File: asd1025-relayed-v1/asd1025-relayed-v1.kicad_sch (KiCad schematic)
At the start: 36 parts, among them J1 Conn_01x09_Female, J10 Conn_01x01_Female, J11 Conn_01x01_Female, J12 Conn_01x01_Female, J13 Conn_01x01_Female, J14 Conn_01x01_Female, J15 Conn_01x01_Female, J16 Conn_01x01_Female, J17 Conn_01x01_Female, J18 Conn_01x01_Female, J19 Conn_01x01_Female, J2 Conn_01x01_Female, J20 Conn_01x01_Female, J21 Conn_01x01_Female, J22 Conn_01x01_Female, J3 Conn_01x01_Female, J4 Conn_01x01_Female, J5 Conn_01x01_Female, J6 Conn_01x01_Female, J7 Conn_01x01_Female, J8 Conn_01x01_Female, J9 Conn_01x01_Female, K1 EC2-4.5NU, K2 EC2-4.5NU, K3 EC2-4.5NU, K4 EC2-4.5NU, K5 EC2-4.5NU, K6 EC2-4.5NU, Q1 BC547, U1 SA555P, U2 74HC02, U3 4017, U4 ULN2004A

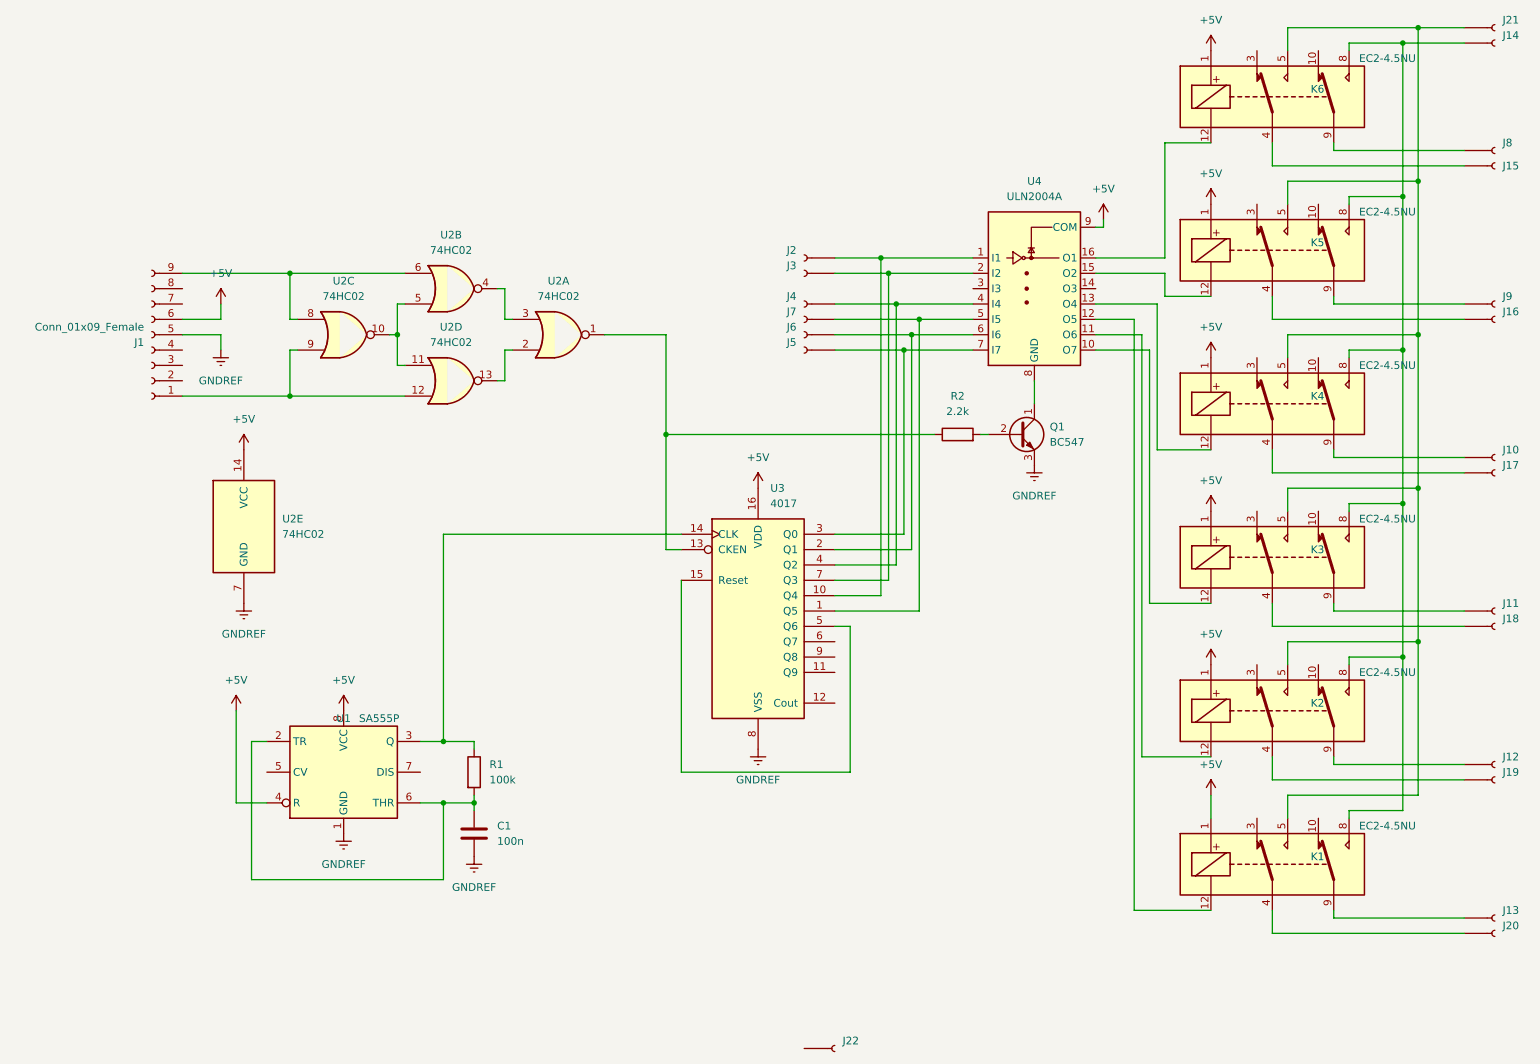
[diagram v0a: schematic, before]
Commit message: fix v1: relays would switch by passing current through base-emittor-resistors in darlington array even if main transistor Q1 is off
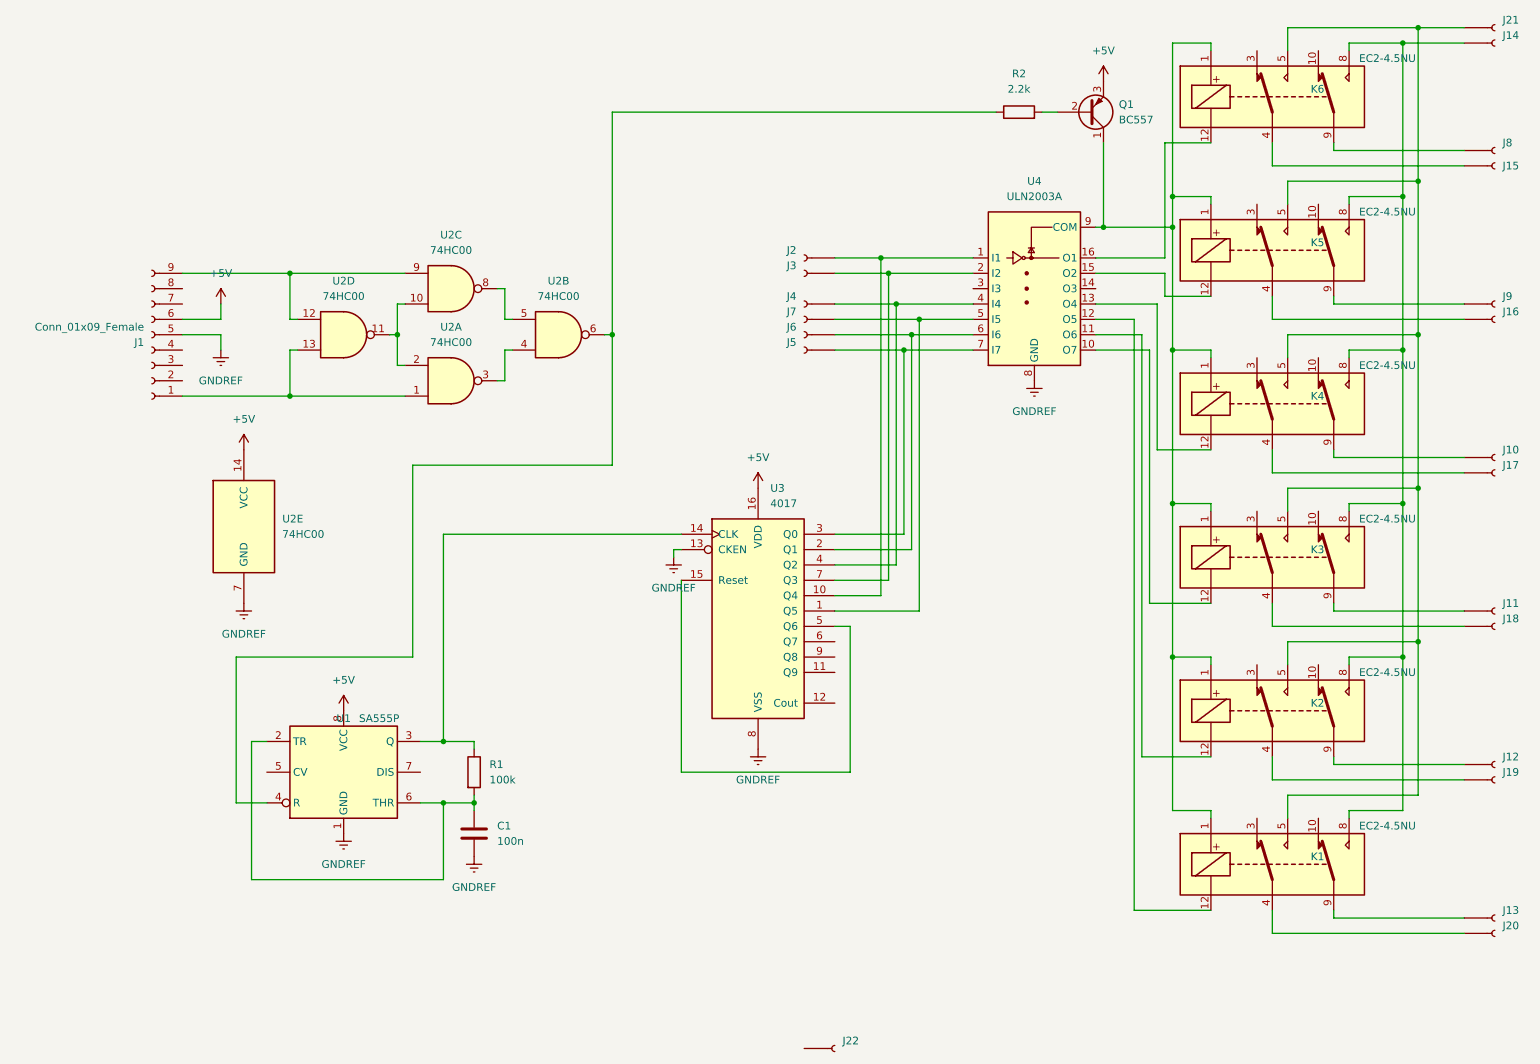
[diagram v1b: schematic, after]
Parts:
- removed Q1: BC547, Package_TO_SOT_THT:TO-92L_Inline_Wide, symbol Transistor_BJT:BC547
- added Q1: BC557, Package_TO_SOT_THT:TO-92_Inline_Wide, symbol Transistor_BJT:BC557
- U2: value 74HC02 -> 74HC00; symbol 74xx:74HC02 -> 74xx:74HC00
- U4: value ULN2004A -> ULN2003A
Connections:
- net +5V: now also Q1.3 (E); no longer K1.1, K2.1, K3.1, K4.1, K5.1, K6.1, U1.4 (R), U4.9 (COM)
- net GNDREF: now also U3.13 (CKEN), U4.8 (GND)
- net at U2.10, U2.11: now also U2.2; no longer U2.5
- net at U2.12, U2.9: now also J1.9 (Pin_9); no longer J1.1 (Pin_1)
- net at U2.13: now also J1.1 (Pin_1), U2.1; no longer U2.2
- net at R2.2: now also Q1.2 (B)
- new net: U2.5, U2.8
- new net: K1.1, K2.1, K3.1, K4.1, K5.1, K6.1, Q1.1 (C), U4.9 (COM)
- new net: R2.1, U1.4 (R), U2.6
